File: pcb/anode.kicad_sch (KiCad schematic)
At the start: 9 parts, among them Q100 Q_NPN_BEC, Q99 Q_NPN_BEC

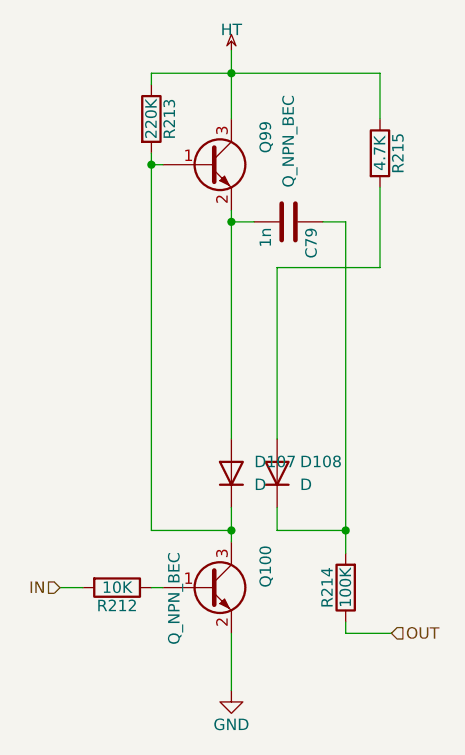
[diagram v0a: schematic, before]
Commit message: Added design files for the kathode, mods to the anode board
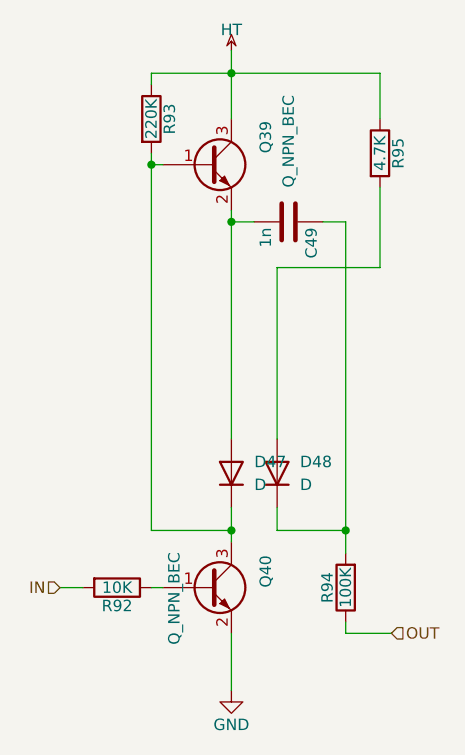
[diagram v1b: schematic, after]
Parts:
- renumbered C79 to C49, D107 to D47, D108 to D48, Q99 to Q39, Q100 to Q40, R212 to R92, R213 to R93, R214 to R94, R215 to R95
